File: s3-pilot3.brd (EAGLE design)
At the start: 86.4 x 49.5 mm, 70 parts, among them IC3 LM1117, IC4 ATMEGA1284, Q1 ZXMP6A13FTA, Q2 2N7002PW, U1 FT231XS, U2 MIC5205, Y2 16MHz

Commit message: .
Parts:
- removed C11, C16: 22p, SparkFun:CAP-PTH-SMALL
- removed C17, C18, C19: 100n, SparkFun:CAP-PTH-SMALL
- removed C20: 4u7, SparkFun:CPOL-RADIAL-10UF-25V
- removed IC4: ATMEGA1284, SteveMarple:DIL40
- removed JP12: PWM3, pinhead:1X03/90
- removed JP13: PWM4, pinhead:1X03/90
- removed L1: 10uH, SteveMarple:RES-AXIAL-0.4
- removed PI_PWR, PI_SW: (no value), pinhead:1X02
- removed Y2: 16MHz, SteveMarple:HC49U-V-RESONATOR
- added C1, C2: 22p, SparkFun:CAP-PTH-SMALL
- added C21: 4u7, SparkFun:CPOL-RADIAL-10UF-25V
- added C8: 100n, SparkFun:CAP-PTH-SMALL
- added IC1: ATMEGA644A, atmel:TQFP44
- added JP14: US2, pinhead:1X04/90
- added JP20: SW_1, pinhead:1X02
- added JP21: 5V_1, pinhead:1X02
- added JP8: MPU-6050, pinhead:1X08
- added Y1: 16MHz, SteveMarple:HC49U-V-RESONATOR
- JP9: value MPU-6050 -> US1; device pinhead:1X08 -> pinhead:1X04/90
- moved JPX1 172.3 mm to (68.6, 58.4)
- moved C6 123.8 mm to (31.8, 45.7), turned to 90 degrees
- moved C15 117.4 mm to (15.2, 40.6), turned to 90 degrees
- moved C3 117.4 mm to (27.9, 40.6), turned to 90 degrees
- moved R3 104.1 mm to (2.54, 16.5), turned to 180 degrees
- moved R1 97.1 mm to (2.54, 20.3), turned to 180 degrees
- moved C10 96.2 mm to (62.2, 69.8)
- moved C12 96.2 mm to (58.4, 69.8)
- moved C13 96.2 mm to (54.6, 69.8)
- moved C14 96.2 mm to (50.8, 69.8)
- moved C9 96.2 mm to (66.0, 69.8)
- moved R11 96.2 mm to (20.3, 69.8)
- moved R12 96.2 mm to (16.5, 69.8)
- moved R13 96.2 mm to (12.7, 69.8)
- moved R14 96.2 mm to (8.89, 69.8)
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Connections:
- removed net 10: IC4.5
- removed net 11(MOSI): IC4.6
- removed net 12(MISO): IC4.7
- removed net 13(SCK): IC4.8
- removed net 14: IC4.29
- removed net 15: IC4.28
- removed net 16(TDI): IC4.27, JTAG.9
- removed net 17(TDO): IC4.26, JTAG.3
- removed net 18(TMS): IC4.25, JTAG.5
- removed net 19(TCK): IC4.24, JTAG.1
- removed net 2(RX1): IC4.16
- removed net 22: IC4.18
- removed net 3(TX1): IC4.17
- removed net 4: IC4.1
- removed net 5: IC4.2
- removed net 6: IC4.3
- removed net 7: IC4.4
- removed net 8: IC4.20
- removed net 9: IC4.19
- removed net A0: IC4.33, JP9.1
- removed net A1: IC4.34
- removed net A2: IC4.35
- removed net A3: IC4.36
- removed net A4: IC4.37
- removed net A5: IC4.38
- removed net A6: IC4.39
- removed net A7: IC4.40
- removed net AREF: C17.1, IC4.32
- removed net N$11: IC4.23, JP9.5
- removed net N$26: IC4.22, JP9.6
- removed net N$40: PI_PWR.2, PI_SW.1
- removed net N$5: C16.1, IC4.13, Y2.2
- removed net N$9: C11.1, IC4.12, Y2.1
- removed net PWM3: JP12.3
- removed net PWM4: JP13.3
- new net JP21: JP20.1, JP21.2
- new net MPU_INT: JP8.1
- new net N$48: C2.1, IC1.8, Y1.2
- new net N$49: C1.1, IC1.7, Y1.1
- new net PISUPPLY: C5.+, D1.C, IC3.3, JP20.2
- new net SCL: IC1.19, JP8.6
- new net SDA: IC1.20, JP8.5
- new net TCK: IC1.21, JTAG.1
- new net TDI: IC1.24, JTAG.9
- new net TDO: IC1.23, JTAG.3
- new net TMS: IC1.22, JTAG.5
- new net US1ECHO: JP14.4, JP9.4
- new net US1TRIG: JP14.3, JP9.3
- new net VCC: IC1.17, IC1.38, IC1.5, JP6.10, JP6.9, JP7.10, JP7.9, JP8.8, JTAG.4
- net !RESET: now also IC1.4; no longer IC4.9
- net 0(RX0): no longer IC4.14
- net 1(TX0): no longer IC4.15
- net 5V: now also C21.1, C8.1; no longer C19.1, C20.1, IC4.10, JP6.10, JP6.9, JP7.10, JP7.9, JP9.8, JTAG.4, L1.P$2
- net AVCC: now also IC1.27; no longer C18.1, IC4.30, L1.P$1
- net GND: now also C1.2, C2.2, C21.2, C8.2, IC1.18, IC1.28, IC1.39, IC1.6, JP14.1, JP21.1, JP8.7, JP9.1, Y1.GND; no longer C11.2, C16.2, C17.2, C18.2, C19.2, C20.2, IC4.11, IC4.31, JP12.1, JP13.1, JP9.7, PI_PWR.1, Y2.GND
- net VIN: now also JP14.2, JP9.2; no longer C5.+, D1.C, IC3.3, JP12.2, JP13.2, PI_SW.2

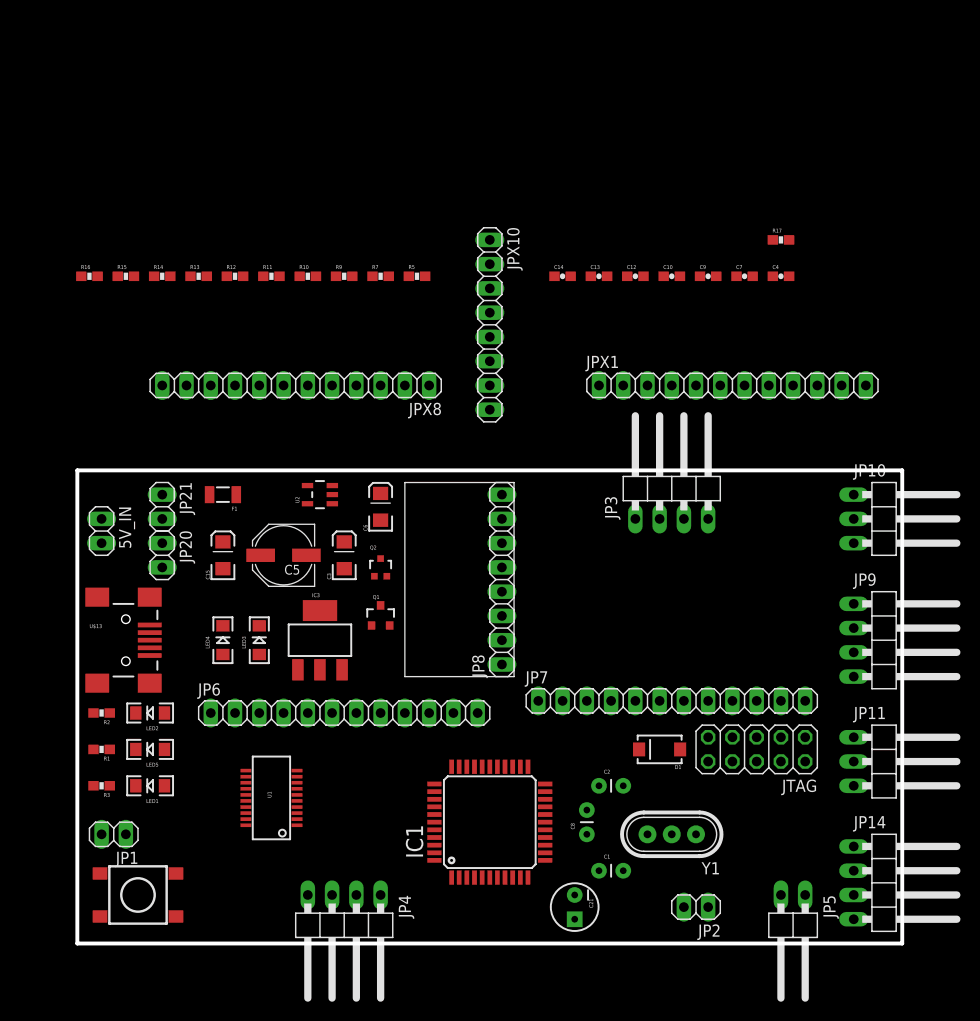
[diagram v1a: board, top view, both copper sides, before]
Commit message: final mounting hole position on bd.
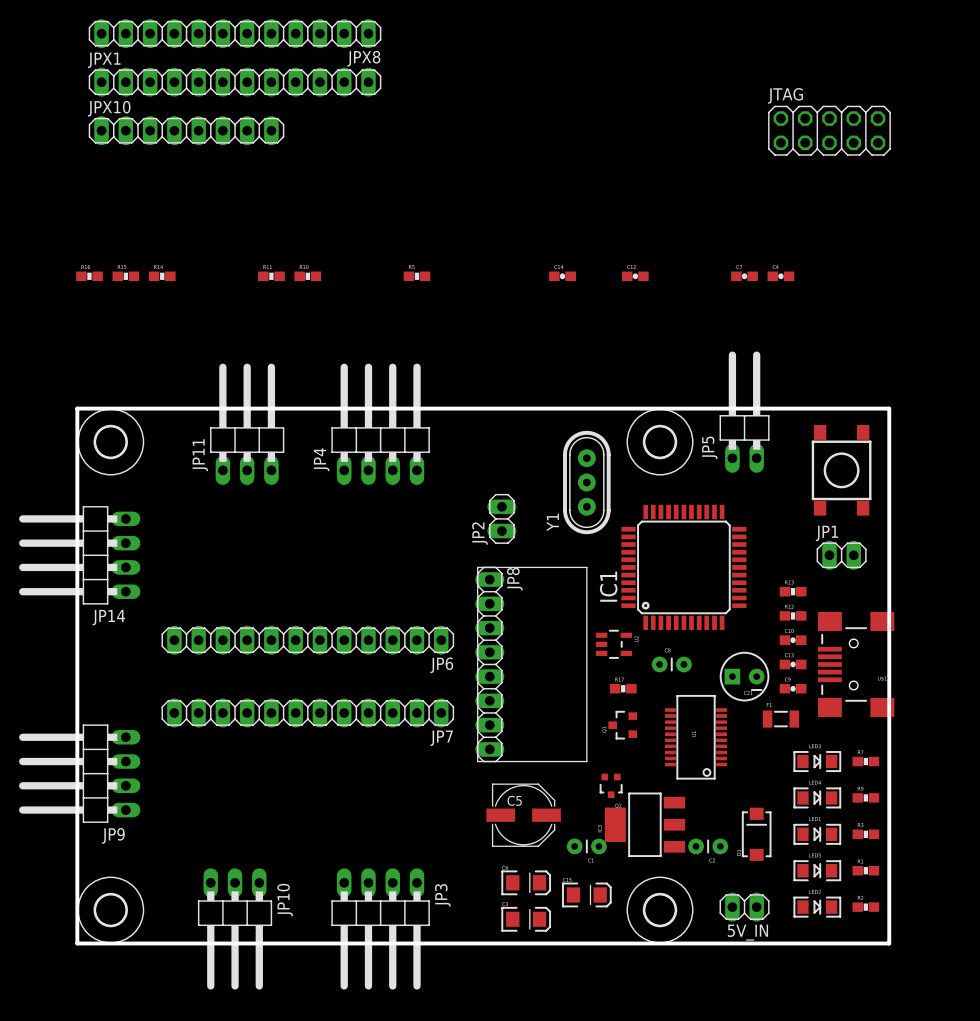
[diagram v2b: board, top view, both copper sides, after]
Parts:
- removed JP20: SW_1, pinhead:1X02
- removed JP21: 5V_1, pinhead:1X02
- added U$2, U$3, U$5, U$6: (no value), holes:3,2
- moved JP14 90.6 mm to (1.27, 40.6), turned to 90 degrees
- moved RESET 86.0 mm to (80.0, 49.5), turned to 270 degrees
- moved JP9 85.0 mm to (1.27, 17.8), turned to 90 degrees
- moved R2 82.5 mm to (82.5, 3.81), turned to 0 degrees
- moved JP1 81.6 mm to (80.0, 40.6), turned to 0 degrees
- moved R1 81.0 mm to (82.5, 7.62), turned to 0 degrees
- moved JP10 80.4 mm to (16.5, 2.54), turned to 180 degrees
- moved R3 80.2 mm to (82.5, 11.4), turned to 0 degrees
- moved 5V_IN 78.0 mm to (69.8, 3.81), turned to 180 degrees
- moved R9 77.2 mm to (82.5, 15.2)
- moved U$13 76.2 mm to (81.3, 29.2), turned to 180 degrees
- moved JP11 75.5 mm to (17.8, 53.3), turned to 0 degrees
- moved LED2 72.7 mm to (77.5, 3.81), turned to 0 degrees
- moved R7 71.8 mm to (82.5, 19.1)
- moved LED5 71.0 mm to (77.5, 7.62), turned to 0 degrees
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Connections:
- removed net JP21: JP20.1, JP21.2
- net GND: no longer JP21.1
- net PISUPPLY: no longer JP20.2
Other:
- board size 86.4 x 49.5 mm -> 85 x 56 mm

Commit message: .
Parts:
- C1, C2, C8: device SparkFun:CAP-PTH-SMALL -> SparkFun:0603-CAP
- C21: device SparkFun:CPOL-RADIAL-10UF-25V -> SparkFun:EIA3216
- JP2: value ESC_ENA -> ENA
- moved JP1 39.4 mm to (41.9, 50.8), turned to 90 degrees
- moved JTAG 39.4 mm to (77.5, 45.7), turned to 90 degrees
- moved C2 38.1 mm to (50.8, 44.5), turned to 270 degrees
- moved RESET 37.4 mm to (68.6, 14.0)
- moved C1 34.9 mm to (48.3, 44.5), turned to 270 degrees
- moved C21 16.7 mm to (53.3, 30.5), turned to 90 degrees
- moved Q2 14.8 mm to (48.3, 29.2), turned to 90 degrees
- moved Q1 14.8 mm to (49.5, 35.6)
- moved D1 13.3 mm to (67.3, 24.1)
- moved U2 10.6 mm to (49.2, 23.3), turned to 90 degrees
- moved R17 10.5 mm to (67.3, 29.2)
- moved R13 7.73 mm to (82.5, 38.1), turned to 90 degrees
- moved U1 5.24 mm to (59.7, 22.9), turned to 0 degrees
- moved Y1 3.59 mm to (50.8, 50.8), turned to 180 degrees
- moved JP2 2.84 mm to (41.9, 45.7)
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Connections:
- net 5V: now also C21.A; no longer C21.1
- net GND: now also C21.C; no longer C21.2
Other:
- board text added: "PilotV3"
- board text added: "Spiked3.com"

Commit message: .
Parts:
- removed 5V_IN: (no value), pinhead:1X02
- removed C2: 22p, SparkFun:0603-CAP
- removed JP1: Reset, pinhead:1X02
- added JP12: PWM3, pinhead:1X03/90
- added U$12, U$15, U$16, U$17: (no value), holes:2,8
- added X1, X2: 5V, con-phoenix-350:1751248
- C1: value 22p -> 47pF; device SparkFun:0603-CAP -> SparkFun-Capacitors:0603-CAP
- moved C1 71.8 mm to (-2.54, -6.35), turned to 0 degrees
- moved JP10 29.0 mm to (2.54, 27.9), turned to 90 degrees
- moved C15 15.9 mm to (39.4, 14.0), turned to 90 degrees
- moved JP11 11.4 mm to (17.8, 41.9)
- moved Y1 7.62 mm to (50.8, 43.2)
- moved C6 3.81 mm to (43.2, 6.35)
- moved JP3 3.81 mm to (27.9, 2.54)
- moved JP4 3.81 mm to (27.9, 53.3)
- moved C3 3.81 mm to (43.2, 2.53)
- moved C9 2.84 mm to (73.7, 27.9), turned to 180 degrees
- moved F1 1.80 mm to (73.0, 24.1)
- moved C13 1.27 mm to (73.7, 30.5)
- moved U$13 1.27 mm to (80.0, 29.2)
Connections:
- net 0(RX0) renamed RX
- net 1(TX0) renamed TX
- removed net N$24: 5V_IN.1, Q1.1, R5.1
- removed net N$36: 5V_IN.2, D1.A
- removed net VCC: IC1.17, IC1.38, IC1.5, JP6.10, JP6.9, JP7.10, JP7.9, JP8.8, JTAG.4
- removed net VIN: JP10.2, JP11.2, JP14.2, JP9.2
- new net N$11: C1.1, U2.4
- new net N$5: Q1.1, R5.1
- new net N$9: D1.A, X1.2, X2.2
- new net PWM3: JP12.3
- net !RESET: no longer JP1.2
- net 5V: now also IC1.17, IC1.38, IC1.5, JP10.2, JP11.2, JP12.2, JP14.2, JP6.10, JP6.9, JP7.10, JP7.9, JP8.8, JP9.2, JTAG.4
- net GND: now also JP12.1, X1.1, X2.1; no longer C2.2, JP1.1
- net N$48: no longer C2.1
- net N$49: no longer C1.1

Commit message: .
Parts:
- removed IC1: ATMEGA644A, atmel:TQFP44
- removed JTAG: (no value), pinhead:2X05
- removed Y1: 16MHz, SteveMarple:HC49U-V-RESONATOR
- added E$2: (no value), holes:3,2
- added IC2: XMEGA16A4A, atmel:TQFP44
- added JP1: (no value), pinhead:1X03
- added Y2: 16MHz, SteveMarple:HC49U-V-RESONATOR
- JP8: value MPU-6050 -> IMU
- U$2: value (none) -> JTAG; device holes:3,2 -> s3-pilot2-lbr:2X5/05
- moved U$2 85.2 mm to (77.5, 45.7), turned to 0 degrees
- moved MPU6050 76.7 mm to (50.8, 95.2), turned to 90 degrees
- moved R16 69.2 mm to (50.8, 21.6)
- moved U$4 66.0 mm to (31.8, 85.1)
- moved C1 62.7 mm to (50.8, 26.7), turned to 180 degrees
- moved U$1 51.2 mm to (53.3, 72.4)
- moved R11 50.8 mm to (50.8, 29.2), turned to 180 degrees
- moved JPX1 50.0 mm to (61.0, 67.3), turned to 180 degrees
- moved R10 46.5 mm to (50.8, 31.8), turned to 180 degrees
- moved R5 42.6 mm to (27.9, 27.9), turned to 180 degrees
- moved C7 42.6 mm to (62.2, 27.9), turned to 90 degrees
- moved C12 41.9 mm to (57.1, 27.9), turned to 90 degrees
- moved R15 37.4 mm to (18.4, 34.9), turned to 180 degrees
- moved R14 32.8 mm to (27.9, 43.2)
- moved JPX10 31.4 mm to (40.6, 96.5)
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- renumbered U$12 to E$12, U$15 to E$15, U$16 to E$16, U$17 to E$17, U$3 to E$3, U$5 to E$5, U$6 to E$6
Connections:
- removed net N$48: IC1.8, Y1.2
- removed net N$49: IC1.7, Y1.1
- new net N$24: JP1.2, Q1.1
- new net N$26: JPX10.8, MPU6050.8
- new net N$36: IC2.36, Y2.2
- new net N$40: IC2.37, Y2.1
- net !RESET: now also IC2.35, U$2.6; no longer IC1.4, JTAG.6
- net 5V: now also IC2.19, IC2.31, IC2.9, U$2.4; no longer IC1.17, IC1.38, IC1.5, JPX10.8, JTAG.4, MPU6050.VCC
- net AVCC: now also IC2.39; no longer IC1.27
- net GND: now also IC2.18, IC2.30, IC2.38, IC2.8, JP1.3, U$2.10, U$2.2, Y2.GND; no longer IC1.18, IC1.28, IC1.39, IC1.6, JTAG.10, JTAG.2, Y1.GND
- net N$1: now also U$4.1; no longer U$4.INV
- net N$13: now also MPU6050.1; no longer MPU6050.INT
- net N$14: now also MPU6050.2; no longer MPU6050.AD0
- net N$16: now also MPU6050.3; no longer MPU6050.XCL
- net N$17: now also MPU6050.4; no longer MPU6050.XDA
- net N$18: now also U$1.1; no longer U$1.INV
- net N$19: now also MPU6050.5; no longer MPU6050.SDA
- net N$20: now also MPU6050.6; no longer MPU6050.SCL
- net N$22: now also MPU6050.7; no longer MPU6050.GND
- net N$25: now also U$1.2; no longer U$1.SLEW
- net N$27: now also U$4.4; no longer U$4.FB
- net N$28: now also U$4.5; no longer U$4.!SF
- net N$29: now also U$4.6; no longer U$4.!PWM!_D1
- net N$3: now also U$4.2; no longer U$4.SLEW
- net N$30: now also U$4.7; no longer U$4.PWM_!D2
- net N$31: now also U$4.8; no longer U$4.IN1
- net N$32: now also U$4.9; no longer U$4.IN2
- net N$33: now also U$4.10; no longer U$4.VDD
- net N$34: now also U$4.11; no longer U$4.GND
- net N$35: now also U$4.12; no longer U$4.VIN
- net N$37: now also U$1.3; no longer U$1.EN
- net N$38: now also U$1.4; no longer U$1.FB
- net N$39: now also U$1.5; no longer U$1.!SF
- net N$4: now also U$4.3; no longer U$4.EN
- net N$41: now also U$1.6; no longer U$1.!PWM!_D1
- net N$42: now also U$1.7; no longer U$1.PWM_!D2
- net N$43: now also U$1.8; no longer U$1.IN1
- net N$44: now also U$1.9; no longer U$1.IN2
- net N$45: now also U$1.10; no longer U$1.VDD
- net N$46: now also U$1.11; no longer U$1.GND
- net N$47: now also U$1.12; no longer U$1.VIN
- net N$5: now also JP1.1; no longer Q1.1
- net RX: now also IC2.20
- net SCL: now also IC2.10; no longer IC1.19
- net SDA: now also IC2.11; no longer IC1.20
- net TCK: now also IC2.12, U$2.1; no longer IC1.21, JTAG.1
- net TDI: now also IC2.15, U$2.9; no longer IC1.24, JTAG.9
- net TDO: now also IC2.14, U$2.3; no longer IC1.23, JTAG.3
- net TMS: now also IC2.13, U$2.5; no longer IC1.22, JTAG.5
- net TX: now also IC2.21
